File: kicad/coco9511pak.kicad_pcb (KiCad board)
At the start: 2 copper layers, 98.3 x 107.1 mm, 37 parts, among them SW1 SW_DIP_x06, U1 74LS32, U10 74LS682, U11 74LS123, U12 74LS05, U13 74LS244, U14 74LS74, U15 PDME2-S5-S12-S, U16 Coco_Cart_Connector, U4 74LS04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

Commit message: Update to v1.1
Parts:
- removed the C15 at (106.9, 86.6)
- removed REF**: WEEE-Logo_5.6x8mm_SilkScreen, Symbol:WEEE-Logo_5.6x8mm_SilkScreen
- removed U15: PDME2-S5-S12-S, Coco:PDME2-S5-S12-S
- added C16: 22uF, Capacitor_THT:CP_Radial_D6.3mm_P2.50mm, F.Cu at (88.9, 94.5)
- added C17: 22uF, Capacitor_THT:CP_Radial_D6.3mm_P2.50mm, F.Cu at (86.4, 84.3)
- added C3: .01uf, Capacitor_THT:C_Axial_L3.8mm_D2.6mm_P7.50mm_Horizontal, F.Cu at (100.3, 108.4)
- added D1: 1N5818, Diode_THT:D_DO-41_SOD81_P10.16mm_Horizontal, F.Cu at (102.1, 80.5)
- added JP2: Jumper_3_Open, Connector_PinHeader_2.54mm:PinHeader_1x03_P2.54mm_Vertical, F.Cu at (77.7, 78.4)
- added L1: 22uH, Inductor_THT:L_Axial_L7.0mm_D3.3mm_P10.16mm_Horizontal_Fastron_MICC, F.Cu at (106.4, 86.1)
- added R5: 215k, Resistor_THT:R_Axial_DIN0207_L6.3mm_D2.5mm_P7.62mm_Horizontal, F.Cu at (111.1, 88.9)
- added R6: 24.9k, Resistor_THT:R_Axial_DIN0207_L6.3mm_D2.5mm_P7.62mm_Horizontal, F.Cu at (111.1, 100.8)
- added R7: 5k, Resistor_THT:R_Axial_DIN0207_L6.3mm_D2.5mm_P7.62mm_Horizontal, F.Cu at (105.9, 101.0)
- added U3: LT1373CN8, Package_DIP:DIP-8_W7.62mm, F.Cu at (96.8, 97.4)
- C15: renamed from C16; value 100pf -> 47pf; footprint Resistor_THT:R_Axial_DIN0207_L6.3mm_D2.5mm_P7.62mm_Horizontal -> Capacitor_THT:C_Axial_L3.8mm_D2.6mm_P7.50mm_Horizontal
- R2: value 2.0k -> 3.3k
- U1, U12, U14, U4, U7, U8, U9: footprint Package_DIP:DIP-14_W7.62mm_Socket -> Package_DIP:DIP-14_W7.62mm
- U10, U13, U6: footprint Package_DIP:DIP-20_W7.62mm_Socket -> Package_DIP:DIP-20_W7.62mm
- U11: footprint Package_DIP:DIP-16_W7.62mm_Socket -> Package_DIP:DIP-16_W7.62mm
- U5: footprint Package_DIP:DIP-24_W15.24mm_Socket -> Package_DIP:DIP-24_W15.24mm
- X1: value CXO 4Mhz -> CXO_DIP14 4Mhz; footprint Package_DIP:DIP-14_W7.62mm_Socket -> Package_DIP:DIP-14_W7.62mm
- moved C12 23.4 mm to (21.5, 137.7), turned to -90 degrees
- moved C1 17.1 mm to (73.0, 101.5)
- moved U1 16.6 mm to (78.4, 109.0)
- moved R1 10.00 mm to (63.0, 101.9), turned to -90 degrees
- moved U5 7.27 mm to (48.6, 97.9)
- moved C2 7.26 mm to (82.8, 87.1)
- moved C5 6.84 mm to (44.1, 93.8)
- moved X1 6.10 mm to (22.1, 94.9)
- moved R4 4.50 mm to (57.8, 101.9), turned to -90 degrees
- moved U12 4.45 mm to (26.3, 145.3)
- moved JP1 2.55 mm to (47.5, 153.3), turned to 0 degrees
- moved C7 0.11 mm to (90.1, 113.2)
- moved U7 0.11 mm to (94.9, 120.8)
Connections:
- net Net-(U5-Pad23) renamed /CLK
- C2 pad 1: VCC -> /+12V
- JP1 pad 1: /HALT* -> Net-(JP1-Pad1)
- JP1 pad 2: Net-(JP1-Pad2) -> /HALT*
- R4 pad 1: Net-(JP1-Pad2) -> Net-(JP1-Pad1)
- U1 pad 1: /E -> /R/W*
- U1 pad 11: /WR* -> unconnected-(U1-Pad11)
- U1 pad 12: Net-(U1-Pad12) -> GND
- U1 pad 13: /PROC_SELECT* -> GND
- U1 pad 2: /Q -> /PROC_SELECT*
- U1 pad 3: Net-(U1-Pad3) -> /WR*
- U1 pad 9: Net-(U1-Pad9) -> /R*/W
- U10 pad 17: GND -> /E
- U10 pad 18: GND -> VCC
- U10 pad 20: +5V -> VCC
- U12 pad 14: GND -> VCC
- U12 pad 3: GND -> Net-(U12-Pad3)
- U12 pad 4: unconnected-(U12-Pad4) -> Net-(JP1-Pad1)
- U12 pad 7: VCC -> GND
- U13 pad 13: /D7 -> /D5
- U13 pad 17: /D5 -> /D7
- U14 pad 1: Net-(U14-Pad1) -> /RESET*
- U14 pad 11: GND -> Net-(U14-Pad11)
- U14 pad 12: GND -> /A0
- U14 pad 3: GND -> Net-(U14-Pad3)
- U14 pad 9: unconnected-(U14-Pad9) -> /C/D*
- U16 pad 2: unconnected-(U16-Pad2) -> /Cart12V
- U16 pad 7: /Q -> unconnected-(U16-Pad7)
- U4 pad 12: unconnected-(U4-Pad12) -> Net-(U14-Pad11)
- U4 pad 13: GND -> /PROC_SELECT*
- U4 pad 8: unconnected-(U4-Pad8) -> Net-(U12-Pad3)
- U4 pad 9: GND -> Net-(U4-Pad9)
- U5 pad 16: Net-(C15-Pad1) (its old number) -> /+12V
- U5 pad 17: Net-(JP1-Pad2) -> Net-(U4-Pad9)
- U5 pad 21: /A0 -> /C/D*
- U6 pad 11: Net-(JP1-Pad2) -> Net-(U14-Pad3)
- U6 pad 15: /D7 -> /D5
- U6 pad 19: /D5 -> /D7
- U7 pad 1: /E -> /LATCH_SELECT
- U7 pad 10: Net-(U7-Pad10) -> GND
- U7 pad 2: /R*/W -> /R/W*
- U7 pad 3: Net-(U1-Pad12) -> /RD_LATCH*
- U7 pad 4: Net-(U1-Pad3) -> (no net)
- U7 pad 5: /R/W* -> (no net)
- U7 pad 6: Net-(U1-Pad9) -> (no net)
- U7 pad 8: /RD_LATCH* -> unconnected-(U7-Pad8)
- U7 pad 9: /LATCH_SELECT -> GND
- U9 pad 1: /RESET* -> /RD_PROC*
- U9 pad 11: Net-(U7-Pad10) -> unconnected-(U9-Pad11)
- U9 pad 12: /E -> GND
- U9 pad 13: /R/W* -> GND
- U9 pad 2: Net-(JP1-Pad2) -> Net-(U4-Pad9)
- U9 pad 3: Net-(U14-Pad1) -> Net-(U14-Pad3)
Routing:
- net Net-(U4-Pad9): track 0.00 -> 165.9 mm
- net /Cart12V: track 0.00 -> 159.9 mm
- net Net-(JP1-Pad2): track 126.9 -> 0.00 mm, vias 1 -> 0
- net /Q: track 102.6 -> 0.00 mm, vias 1 -> 0
- net Net-(U14-Pad3): track 0.00 -> 101.4 mm
- net /C/D*: track 0.00 -> 99.1 mm, vias 0 -> 1
- net Net-(U7-Pad10): track 95.0 -> 0.00 mm
- net Net-(U12-Pad3): track 0.00 -> 88.5 mm
- net Net-(JP1-Pad1): track 0.00 -> 84.9 mm
- net /E: track 139.7 -> 64.2 mm, vias 1 -> 0
- net /A0: track 85.3 -> 18.5 mm
- net Net-(U14-Pad11): track 0.00 -> 48.7 mm, vias 0 -> 1
- net /RESET*: track 125.0 -> 80.0 mm, vias 1 -> 2
- net VCC: track 373.7 -> 335.1 mm
- net Net-(C17-Pad1): track 0.00 -> 38.0 mm
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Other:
- board text added: "+12V Source"
- board text added: "AM9511 Pak for Color Computer v1.1 Copyright 2023 Don Barber License GPLv3 https://github.com/barberd/coco9511pak"
- board text added: "Cart"
- board text added: "Circuit"
- board text removed: "AM9511 Pak for Color Computer v1.00 Copyright 2023 Don Barber License GPLv3 https://github.com/barberd/coco9511pak"

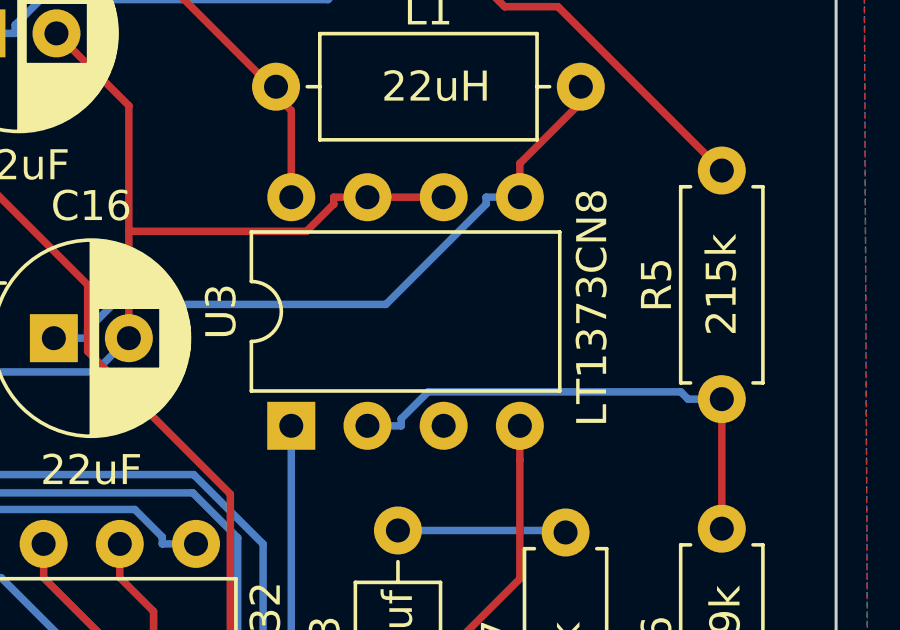
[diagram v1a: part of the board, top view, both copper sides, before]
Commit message: Fixed missing vcc in boost circuit
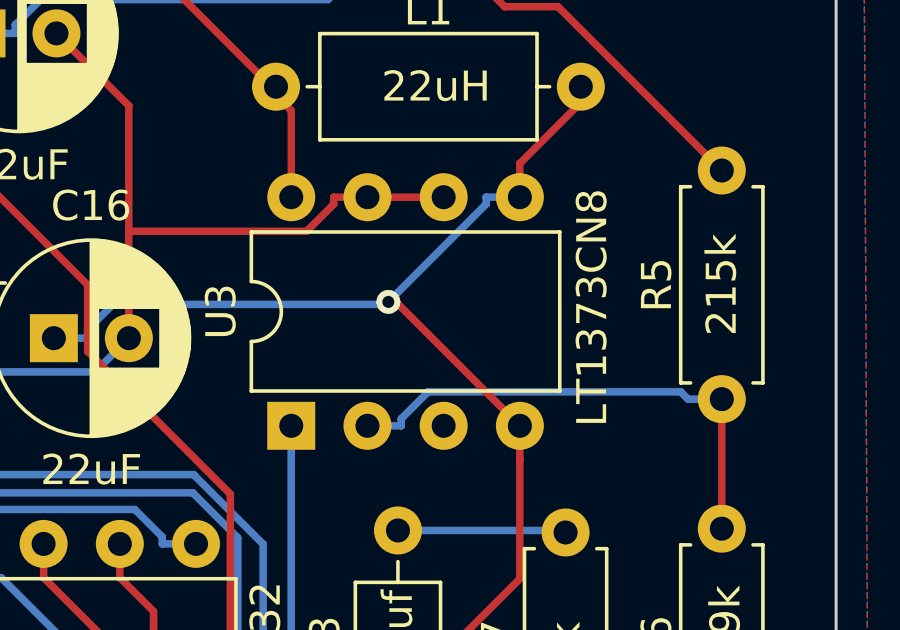
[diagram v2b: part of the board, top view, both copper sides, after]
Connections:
- C16 pad 1: Net-(C16-Pad1) -> VCC
- L1 pad 1: Net-(C16-Pad1) -> VCC
- U3 pad 5: Net-(C16-Pad1) -> VCC
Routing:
- net VCC: track 335.1 -> 363.5 mm, vias 1 -> 2
- net Net-(C16-Pad1): track 22.3 -> 0.00 mm

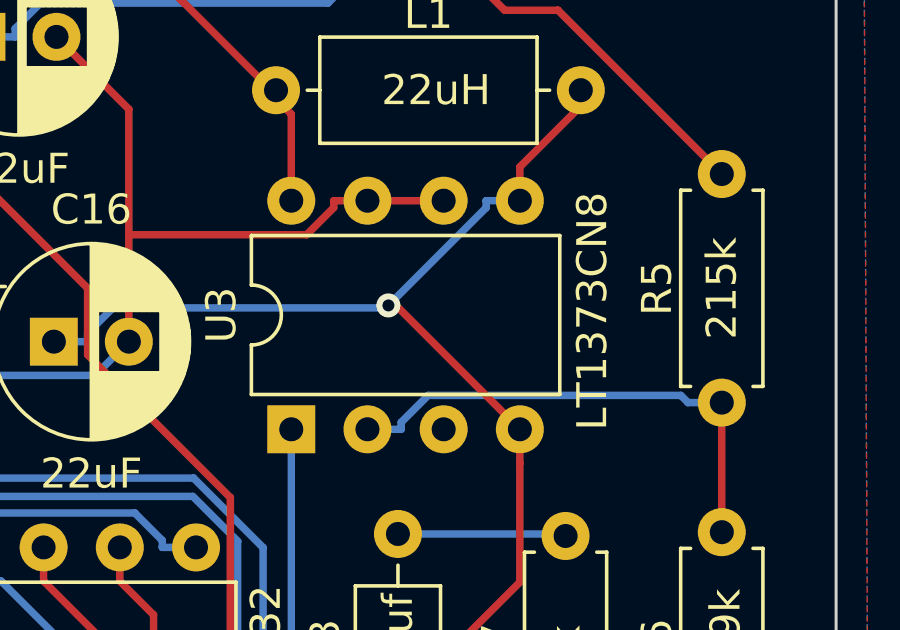
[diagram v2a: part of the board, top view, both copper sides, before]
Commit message: Fixed vcc in boost circuit
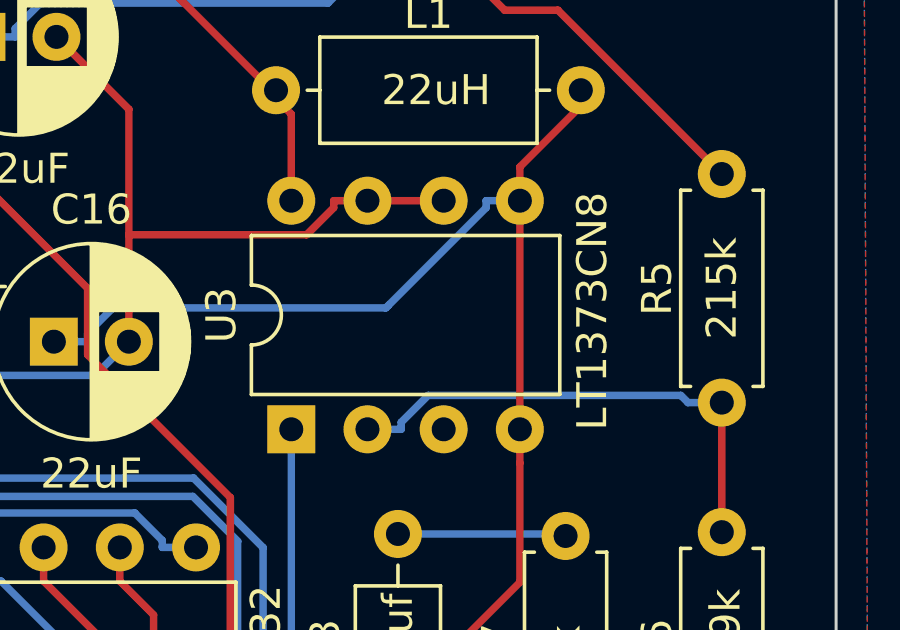
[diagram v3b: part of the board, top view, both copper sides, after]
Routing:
- net VCC: track 363.5 -> 365.0 mm, vias 2 -> 1
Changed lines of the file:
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@@
   (segment (start 91.2332 123.9358) (end 90.201 124.968) (width 0.25) (layer "F.Cu") (net 1))
   (segment (start 27.051 125.476) (end 25.9216 126.6054) (width 0.25) (layer "F.Cu") (net 1))
-  (segment (start 100.265 93.28) (end 104.394 97.409) (width 0.25) (layer "F.Cu") (net 1))
   (segment (start 44.069 93.793) (end 46.6452 93.793) (width 0.25) (layer "F.Cu") (net 1))
   (segment (start 92.456 137.287) (end 92.456 136.1619) (width 0.25) (layer "F.Cu") (net 1))
@@
   (segment (start 29.327 122.4725) (end 29.327 123.0351) (width 0.25) (layer "F.Cu") (net 1))
   (segment (start 26.289 137.658) (end 26.289 136.5329) (width 0.25) (layer "F.Cu") (net 1))
-  (segment (start 100.011 93.28) (end 100.265 93.28) (width 0.25) (layer "F.Cu") (net 1))
   (segment (start 58.034 150.104) (end 60.574 150.104) (width 0.25) (layer "F.Cu") (net 1))
   (segment (start 25.1638 139.9083) (end 26.289 138.7831) (width 0.25) (layer "F.Cu") (net 1))
@@
   (segment (start 44.567 114.29) (end 45.6921 114.29) (width 0.25) (layer "F.Cu") (net 1))
   (segment (start 91.2332 114.3062) (end 91.2332 123.9358) (width 0.25) (layer "F.Cu") (net 1))
+  (segment (start 104.394 97.409) (end 104.394 89.789) (width 0.25) (layer "F.Cu") (net 1))
   (segment (start 106.426 86.6319) (end 106.426 86.106) (width 0.25) (layer "F.Cu") (net 1))
   (segment (start 80.3854 102.4805) (end 83.6348 102.4805) (width 0.25) (layer "F.Cu") (net 1))
@@
   (segment (start 29.327 123.0351) (end 27.051 125.3111) (width 0.25) (layer "F.Cu") (net 1))
   (via (at 50.8824 152.5091) (size 0.8) (drill 0.4) (layers "F.Cu" "B.Cu") (net 1))
-  (via (at 100.011 93.28) (size 0.8) (drill 0.4) (layers "F.Cu" "B.Cu") (net 1))
   (segment (start 21.971 114.3) (end 25.6519 114.3) (width 0.25) (layer "B.Cu") (net 1))
   (segment (start 53.721 113.157) (end 57.2899 113.157) (width 0.25) (layer "B.Cu") (net 1))

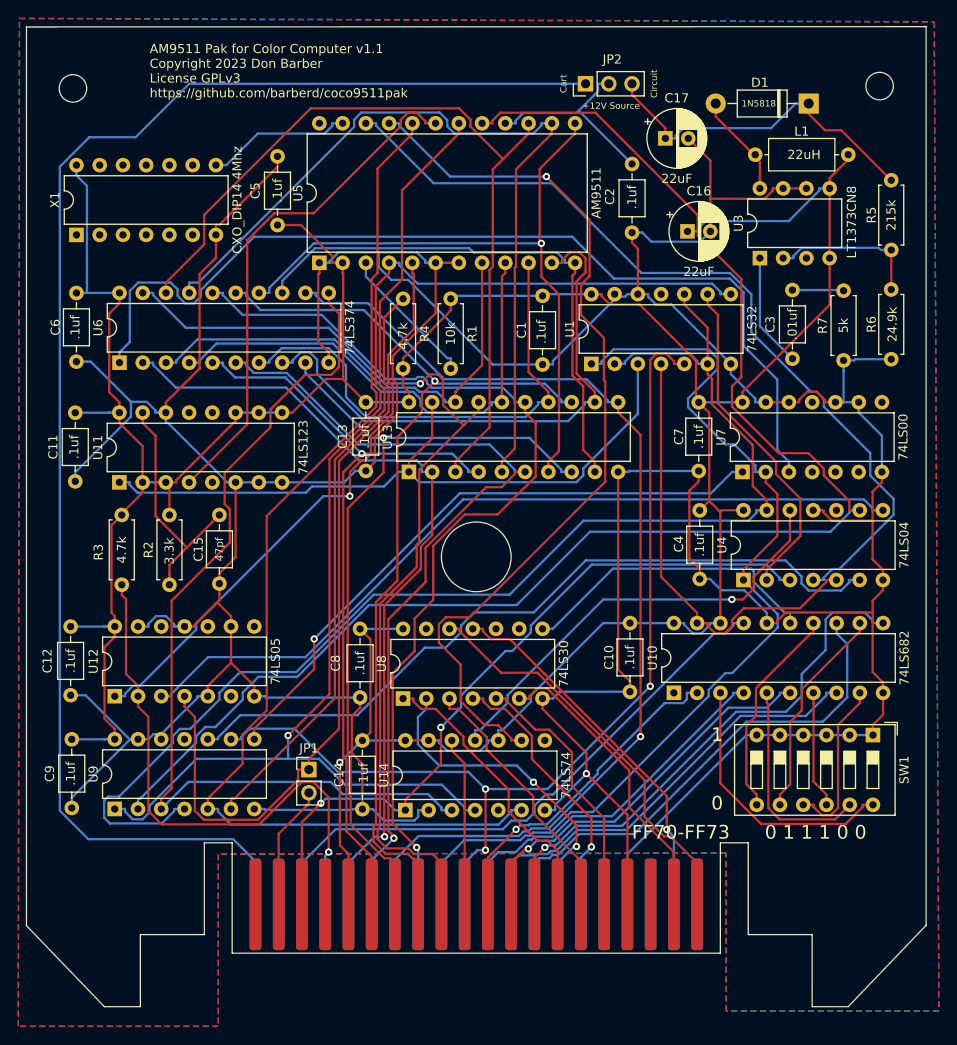
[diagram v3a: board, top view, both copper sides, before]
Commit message: Minor update to silkscreening
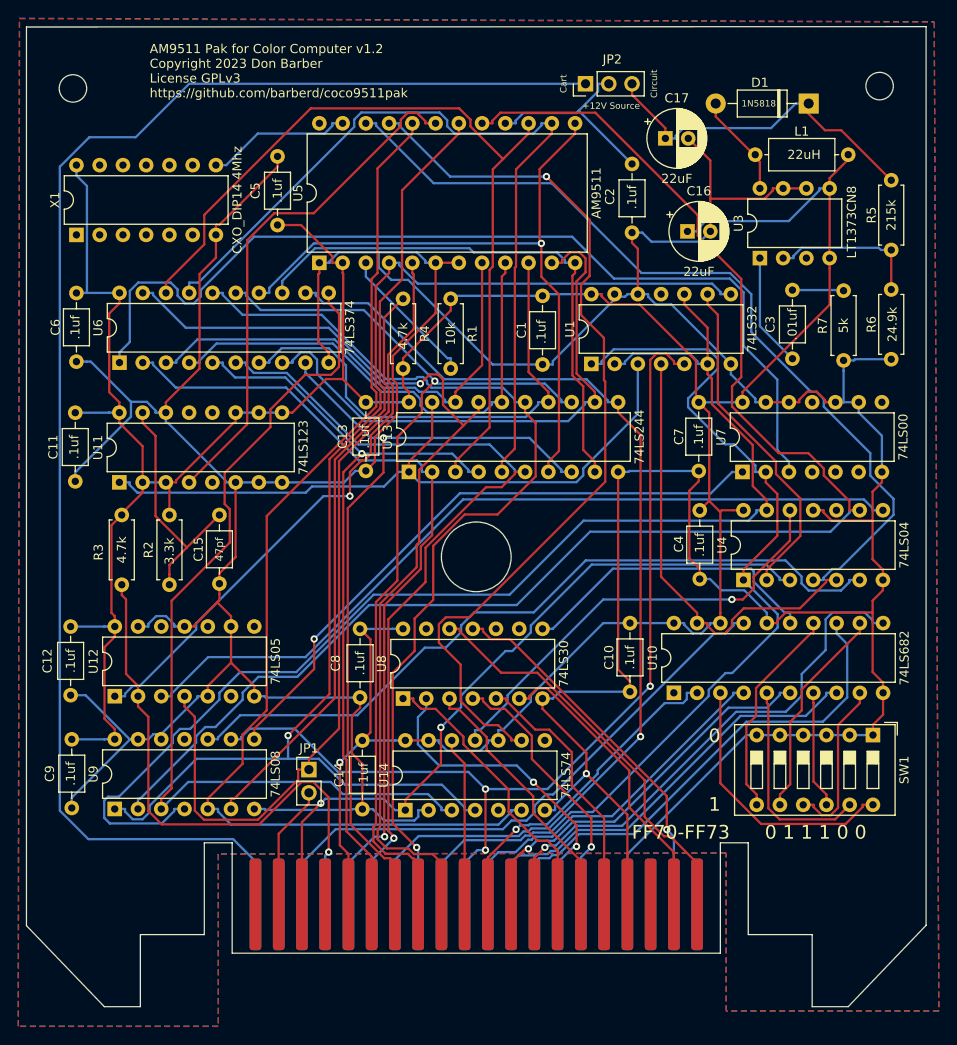
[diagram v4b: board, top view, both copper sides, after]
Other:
- board text added: "AM9511 Pak for Color Computer v1.2 Copyright 2023 Don Barber License GPLv3 https://github.com/barberd/coco9511pak"
- board text removed: "AM9511 Pak for Color Computer v1.1 Copyright 2023 Don Barber License GPLv3 https://github.com/barberd/coco9511pak"
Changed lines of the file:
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@@
       (effects (font (size 1 1) (thickness 0.15)))
     )
-    (fp_text value "74LS08" (at 3.81 17.57 90) (layer "F.Fab")
+    (fp_text value "74LS08" (at 3.81 17.57 90) (layer "F.SilkS")
       (effects (font (size 1 1) (thickness 0.15)))
     )
@@
       (effects (font (size 1 1) (thickness 0.15)))
     )
-    (fp_text value "74LS244" (at 3.81 25.19 90) (layer "F.Fab")
+    (fp_text value "74LS244" (at 3.81 25.19 90) (layer "F.SilkS")
       (effects (font (size 1 1) (thickness 0.15)))
     )
@@
   (gr_circle (center 109.855 78.613) (end 111.355 78.613) (layer "Edge.Cuts") (width 0.1) (fill none))
   (gr_line (start 29.083 171.323) (end 29.083 179.197) (layer "Edge.Cuts") (width 0.1))
-  (gr_text "0" (at 92.106 156.972) (layer "F.SilkS")
+  (gr_text "0" (at 91.821 149.606) (layer "F.SilkS")
     (effects (font (size 1.5 1.5) (thickness 0.3)))
   )
-  (gr_text "AM9511 Pak for Color Computer v1.1\nCopyright 2023 Don Barber\nLicense GPLv3\nhttps://github.com/barberd/coco9511pak" (at 30.099 76.962) (layer "F.SilkS")
+  (gr_text "AM9511 Pak for Color Computer v1.2\nCopyright 2023 Don Barber\nLicense GPLv3\nhttps://github.com/barberd/coco9511pak" (at 30.099 76.962) (layer "F.SilkS")
     (effects (font (size 1 1) (thickness 0.25)) (justify left))
   )
@@
     (effects (font (size 0.7 0.7) (thickness 0.175)))
   )
-  (gr_text "1" (at 92.106 149.479) (layer "F.SilkS")
+  (gr_text "1" (at 91.821 157.099) (layer "F.SilkS")
     (effects (font (size 1.5 1.5) (thickness 0.3)))
   )
